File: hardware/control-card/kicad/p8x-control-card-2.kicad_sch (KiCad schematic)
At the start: 9 parts, among them U10 28C64, U11 28C64, U12 28C64, U13 28C64, U14 74HCT374, U15 74HCT374, U16 74HCT374, U17 74HCT374, U18 74HCT161

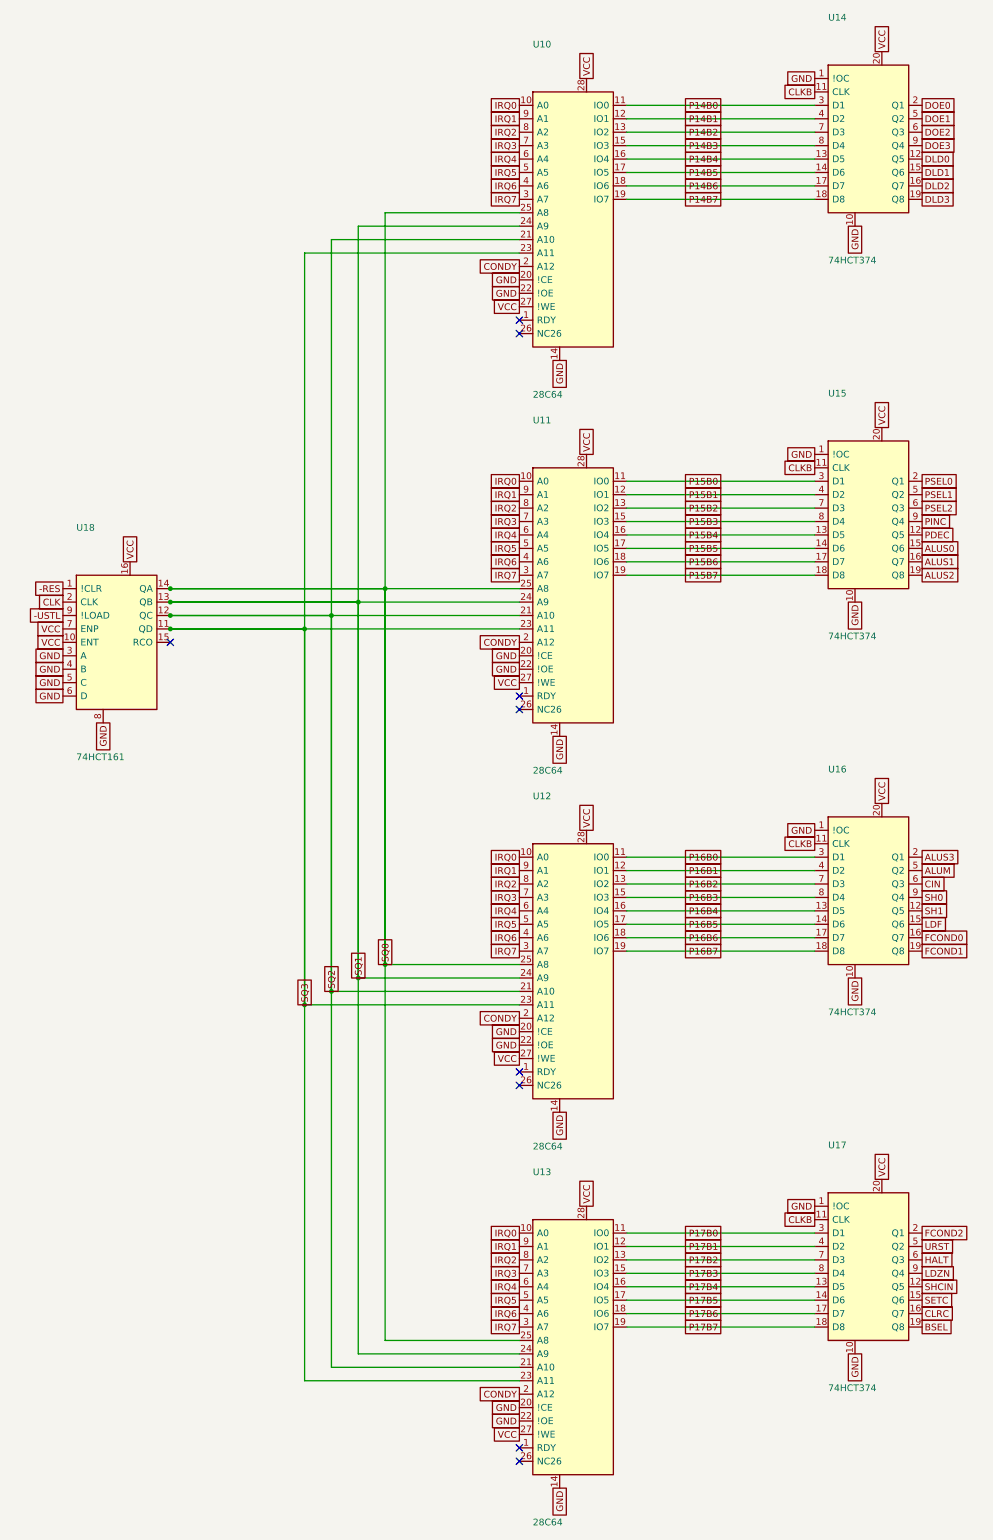
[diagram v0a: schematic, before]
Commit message: feat(sch): draw every P8X card schematic by function
Extend the functional-sheet grouping from the io-card to the control,
regbank, alu, memory, cf, ps2 and bustest cards. functional_sheets now
attaches unnamed glue gates, LEDs, resistors and connectors to the block
they share the most local nets with, so each block lists only its main
parts. A net with two or more pins on a sheet is now wired there even if
it continues elsewhere (its global name label rides on the wire), and
every wire is oriented by drawing side. The regbank gets one pointer per
sheet; the ps2 latches share a sheet with the AVR so the mailbox bus is
drawn. The bustest probe resistors use a straight-order RNISO8DSTR
drawing (the reversed B side forced every wire to cross and the sheet
fell back to labels). build_sch.sh now shows ELK fallbacks and clears old
numbered sheets before a build. All eight netlists match the boards,
ERC 0 errors; the boards change only in footprint link paths.

Co-Authored-By: Claude Opus 5.5 <noreply@anthropic.com>
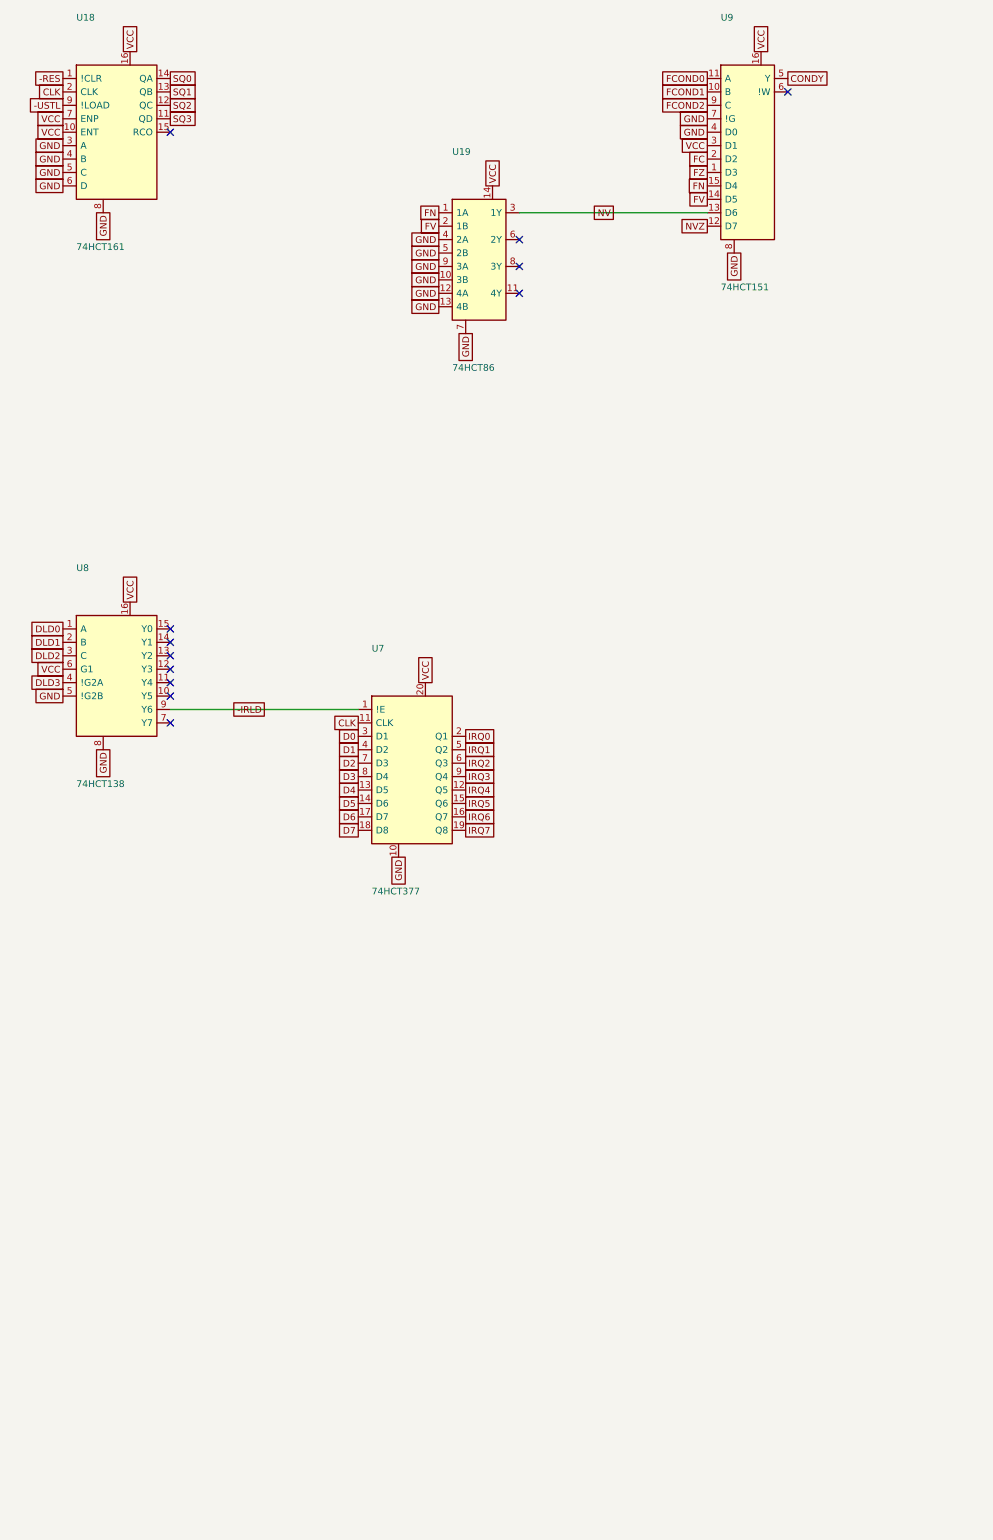
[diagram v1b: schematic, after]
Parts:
- removed U10, U11, U12, U13: 28C64, Package_DIP:DIP-28_W15.24mm, symbol p8x:28C64
- removed U14, U15, U16, U17: 74HCT374, Package_DIP:DIP-20_W7.62mm, symbol p8x:74374
- added U19: 74HCT86, Package_DIP:DIP-14_W7.62mm, symbol p8x:GATES14
- added U7: 74HCT377, Package_DIP:DIP-20_W7.62mm, symbol p8x:74377V2
- added U8: 74HCT138, Package_DIP:DIP-16_W7.62mm, symbol p8x:74138
- added U9: 74HCT151, Package_DIP:DIP-16_W7.62mm, symbol p8x:74151
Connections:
- net CLK: now also U7.11 (CLK)
- net CONDY: now also U9.5 (Y)
- net DLD0: now also U8.1 (A)
- net DLD1: now also U8.2 (B)
- net DLD2: now also U8.3 (C)
- net DLD3: now also U8.4 (!G2A)
- net FCOND0: now also U9.11 (A)
- net FCOND1: now also U9.10 (B)
- net FCOND2: now also U9.9 (C)
- net GND: now also U19.10 (3B), U19.12 (4A), U19.13 (4B), U19.4 (2A), U19.5 (2B), U19.7, U19.9 (3A), U7.10, U8.5 (!G2B), U8.8, U9.4 (D0), U9.7 (!G), U9.8
- net IRQ0: now also U7.2 (Q1)
- net IRQ1: now also U7.5 (Q2)
- net IRQ2: now also U7.6 (Q3)
- net IRQ3: now also U7.9 (Q4)
- net IRQ4: now also U7.12 (Q5)
- net IRQ5: now also U7.15 (Q6)
- net IRQ6: now also U7.16 (Q7)
- net IRQ7: now also U7.19 (Q8)
- net VCC: now also U19.14, U7.20, U8.16, U8.6 (G1), U9.16, U9.3 (D1)
- new net -IRLD: U7.1 (!E), U8.9 (Y6)
- new net D0: U7.3 (D1)
- new net D1: U7.4 (D2)
- new net D2: U7.7 (D3)
- new net D3: U7.8 (D4)
- new net D4: U7.13 (D5)
- new net D5: U7.14 (D6)
- new net D6: U7.17 (D7)
- new net D7: U7.18 (D8)
- new net FC: U9.2 (D2)
- new net FN: U19.1 (1A), U9.15 (D4)
- new net FV: U19.2 (1B), U9.14 (D5)
- new net FZ: U9.1 (D3)
- new net NV: U19.3 (1Y), U9.13 (D6)
- new net NVZ: U9.12 (D7)
- no-connect marks 9 -> 12
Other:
- moved on the sheet: U18
